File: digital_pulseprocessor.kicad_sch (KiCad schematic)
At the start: 26 parts, among them U300 SN74LV221AD, U301 SN74LV221AD, U305 74AC151M n.b.

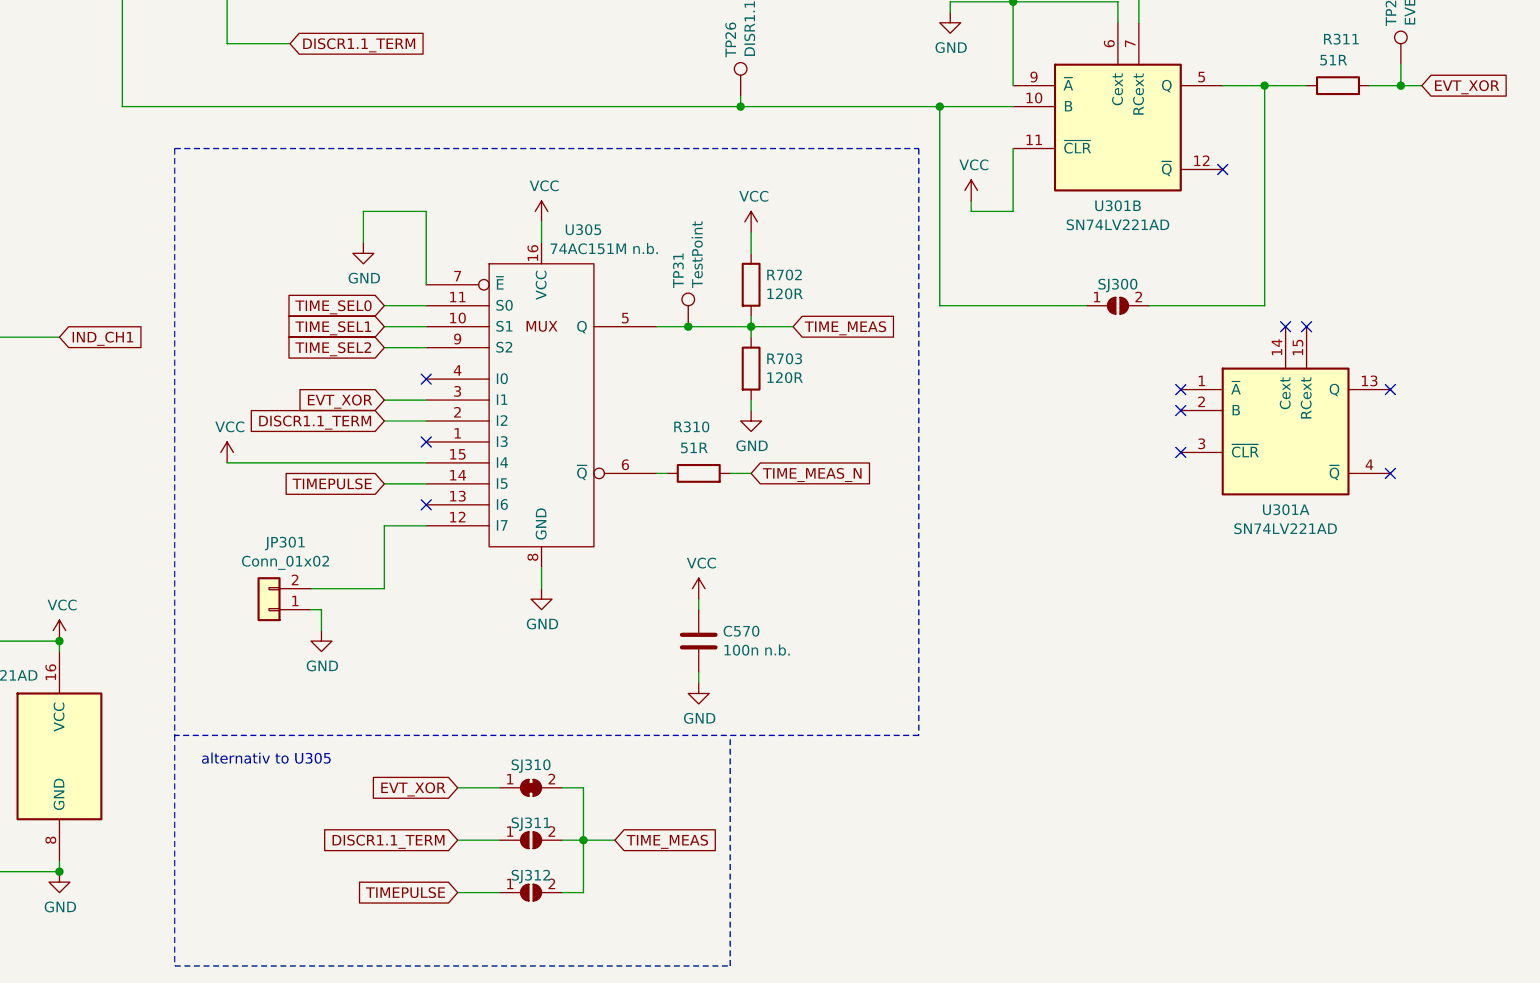
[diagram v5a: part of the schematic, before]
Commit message: Removed optionals parts. Cleaned up Schematics
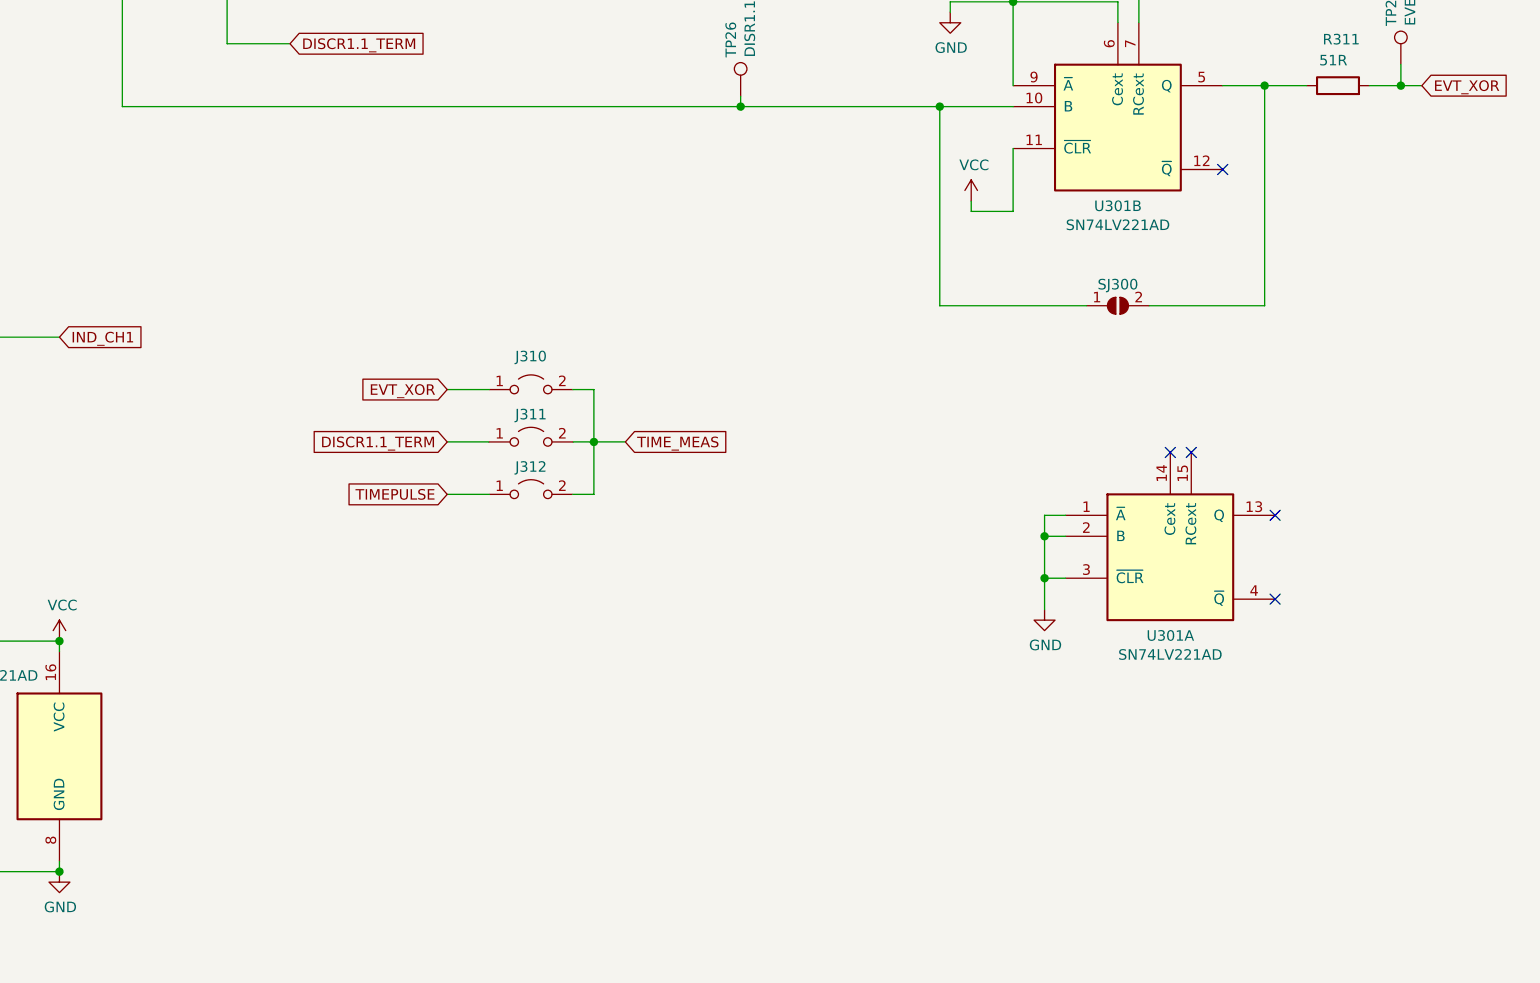
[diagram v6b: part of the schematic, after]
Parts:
- removed C570: 100n n.b., Capacitor_SMD:C_0805_2012Metric_Pad1.18x1.45mm_HandSolder, symbol Device:C
- removed JP301: Conn_01x02, Connector_PinHeader_2.54mm:PinHeader_1x02_P2.54mm_Vertical, symbol Connector_Generic:Conn_01x02
- removed R310: 51R, Resistor_SMD:R_0805_2012Metric_Pad1.20x1.40mm_HandSolder, symbol Device:R
- removed R702, R703: 120R, Resistor_SMD:R_0805_2012Metric_Pad1.20x1.40mm_HandSolder, symbol Device:R
- removed TP31: TestPoint, TestPoint:TestPoint_THTPad_1.5x1.5mm_Drill0.7mm, symbol Connector:TestPoint
- removed U305: 74AC151M n.b., Package_SO:SOP-16_3.9x9.9mm_P1.27mm, symbol muonpi-kicad-library:74AC151M
- J310: renamed from SJ310; footprint Jumper:SolderJumper-2_P1.3mm_Bridged_Pad1.0x1.5mm -> Connector_PinHeader_2.54mm:PinHeader_1x02_P2.54mm_Vertical; symbol Jumper:SolderJumper_2_Bridged -> Jumper:Jumper_2_Open; now in the parts list
- J311: renamed from SJ311; footprint Jumper:SolderJumper-2_P1.3mm_Open_Pad1.0x1.5mm -> Connector_PinHeader_2.54mm:PinHeader_1x02_P2.54mm_Vertical; symbol Jumper:SolderJumper_2_Open -> Jumper:Jumper_2_Open; now in the parts list
- J312: renamed from SJ312; footprint Jumper:SolderJumper-2_P1.3mm_Open_Pad1.0x1.5mm -> Connector_PinHeader_2.54mm:PinHeader_1x02_P2.54mm_Vertical; symbol Jumper:SolderJumper_2_Open -> Jumper:Jumper_2_Open; now in the parts list
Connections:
- net GND: now also U301.1 (~A), U301.2 (B), U301.3 (~CLR)
- no-connect marks 13 -> 7
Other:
- note removed: "alternativ to U305"
- moved on the sheet: U301A

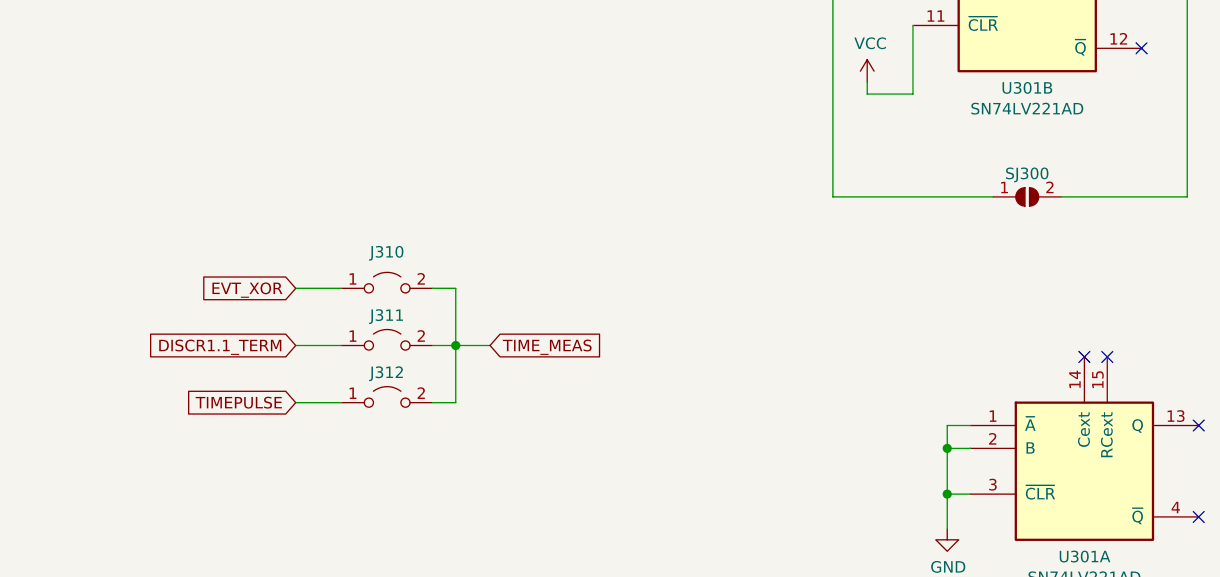
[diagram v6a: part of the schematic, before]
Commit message: Cleand all errors and warnings. Ready for review
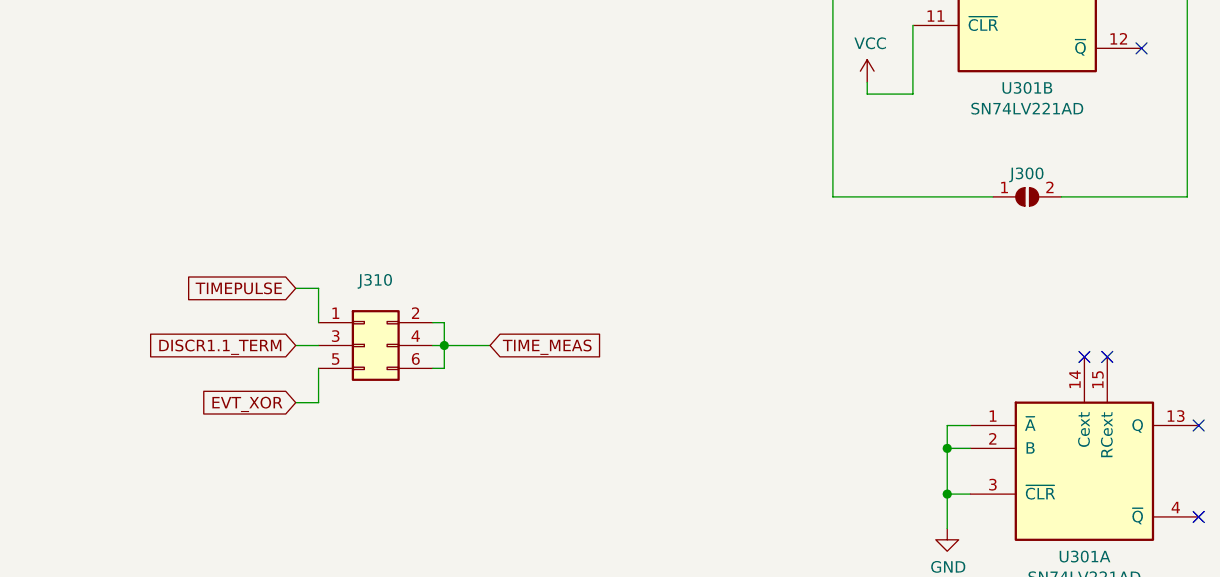
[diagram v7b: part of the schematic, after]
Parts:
- removed J310: Jumper_NC_Small, Connector_PinHeader_2.54mm:PinHeader_1x02_P2.54mm_Vertical, symbol Jumper:Jumper_2_Open
- removed J311, J312: Jumper_NO_Small, Connector_PinHeader_2.54mm:PinHeader_1x02_P2.54mm_Vertical, symbol Jumper:Jumper_2_Open
- added J310: Conn_02x03_Odd_Even, Connector_PinHeader_2.54mm:PinHeader_2x03_P2.54mm_Vertical, symbol Connector_Generic:Conn_02x03_Odd_Even
- J300: renamed from SJ300; now left out of the parts list
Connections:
- net DISCR1.1_TERM: now also J310.3 (Pin_3)
- net EVT_XOR: now also J310.5 (Pin_5)
- net TIMEPULSE: now also J310.1 (Pin_1)
- net TIME_MEAS: now also J310.2 (Pin_2), J310.4 (Pin_4), J310.6 (Pin_6)
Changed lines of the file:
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@@
   (junction (at 114.3 57.15) (diameter 1.016) (color 0 0 0 0))
   (junction (at 114.3 71.12) (diameter 1.016) (color 0 0 0 0))
-  (junction (at 158.75 129.54) (diameter 1.016) (color 0 0 0 0))
+  (junction (at 157.48 129.54) (diameter 1.016) (color 0 0 0 0))
   (junction (at 176.53 88.9) (diameter 1.016) (color 0 0 0 0))
   (junction (at 200.66 88.9) (diameter 1.016) (color 0 0 0 0))
@@
     (stroke (width 0) (type solid) (color 0 0 0 0))
   )
-  (wire (pts (xy 140.97 123.19) (xy 146.05 123.19))
-    (stroke (width 0) (type solid) (color 0 0 0 0))
-  )
-  (wire (pts (xy 140.97 129.54) (xy 146.05 129.54))
-    (stroke (width 0) (type solid) (color 0 0 0 0))
-  )
-  (wire (pts (xy 140.97 135.89) (xy 146.05 135.89))
-    (stroke (width 0) (type solid) (color 0 0 0 0))
-  )
-  (wire (pts (xy 156.21 123.19) (xy 158.75 123.19))
-    (stroke (width 0) (type solid) (color 0 0 0 0))
-  )
-  (wire (pts (xy 156.21 129.54) (xy 158.75 129.54))
-    (stroke (width 0) (type solid) (color 0 0 0 0))
-  )
-  (wire (pts (xy 156.21 135.89) (xy 158.75 135.89))
-    (stroke (width 0) (type solid) (color 0 0 0 0))
-  )
-  (wire (pts (xy 158.75 123.19) (xy 158.75 129.54))
-    (stroke (width 0) (type solid) (color 0 0 0 0))
-  )
-  (wire (pts (xy 158.75 129.54) (xy 158.75 135.89))
-    (stroke (width 0) (type solid) (color 0 0 0 0))
-  )
-  (wire (pts (xy 158.75 129.54) (xy 162.56 129.54))
+  (wire (pts (xy 140.97 123.19) (xy 143.51 123.19))
+    (stroke (width 0) (type solid) (color 0 0 0 0))
+  )
+  (wire (pts (xy 140.97 129.54) (xy 143.51 129.54))
+    (stroke (width 0) (type solid) (color 0 0 0 0))
+  )
+  (wire (pts (xy 140.97 135.89) (xy 143.51 135.89))
+    (stroke (width 0) (type solid) (color 0 0 0 0))
+  )
+  (wire (pts (xy 143.51 123.19) (xy 143.51 127))
+    (stroke (width 0) (type solid) (color 0 0 0 0))
+  )
+  (wire (pts (xy 143.51 135.89) (xy 143.51 132.08))
+    (stroke (width 0) (type solid) (color 0 0 0 0))
+  )
+  (wire (pts (xy 156.21 127) (xy 157.48 127))
+    (stroke (width 0) (type solid) (color 0 0 0 0))
+  )
+  (wire (pts (xy 156.21 129.54) (xy 157.48 129.54))
+    (stroke (width 0) (type solid) (color 0 0 0 0))
+  )
+  (wire (pts (xy 156.21 132.08) (xy 157.48 132.08))
+    (stroke (width 0) (type solid) (color 0 0 0 0))
+  )
+  (wire (pts (xy 157.48 127) (xy 157.48 129.54))
+    (stroke (width 0) (type solid) (color 0 0 0 0))
+  )
+  (wire (pts (xy 157.48 129.54) (xy 162.56 129.54))
+    (stroke (width 0) (type solid) (color 0 0 0 0))
+  )
+  (wire (pts (xy 157.48 132.08) (xy 157.48 129.54))
     (stroke (width 0) (type solid) (color 0 0 0 0))
   )
@@
     )
   )
-  (global_label "EVT_XOR" (shape input) (at 140.97 123.19 180)
+  (global_label "TIMEPULSE" (shape input) (at 140.97 123.19 180)
     (effects (font (size 1.27 1.27)) (justify right))
-    (property "Intersheet References" "${INTERSHEET_REFS}" (id 0) (at 129.05 123.2694 0)
+    (property "Intersheet References" "${INTERSHEET_REFS}" (id 0) (at 126.8729 123.1106 0)
       (effects (font (size 1.27 1.27)) (justify right) hide)
     )
@@
     )
   )
-  (global_label "TIMEPULSE" (shape input) (at 140.97 135.89 180)
+  (global_label "EVT_XOR" (shape input) (at 140.97 135.89 180)
     (effects (font (size 1.27 1.27)) (justify right))
-    (property "Intersheet References" "${INTERSHEET_REFS}" (id 0) (at 126.8729 135.8106 0)
+    (property "Intersheet References" "${INTERSHEET_REFS}" (id 0) (at 129.05 135.9694 0)
       (effects (font (size 1.27 1.27)) (justify right) hide)
     )
@@
   )
   (symbol (lib_id "Jumper:SolderJumper_2_Open") (at 222.25 113.03 0) (unit 1)
-    (in_bom yes) (on_board yes)
-    (property "Reference" "SJ300" (id 0) (at 222.25 110.4646 0))
+    (in_bom no) (on_board yes)
+    (property "Reference" "J300" (id 0) (at 222.25 110.4646 0))
     (property "Value" "SolderJumper_2_Open" (id 1) (at 222.25 110.236 0)
       (effects (font (size 1.27 1.27)) hide)
@@
     (pin "2")
   )
-  (symbol (lib_id "Jumper:Jumper_2_Open") (at 151.13 123.19 0) (unit 1)
-    (in_bom yes) (on_board yes)
-    (property "Reference" "J310" (id 0) (at 151.13 119.1768 0))
-    (property "Value" "Jumper_NC_Small" (id 1) (at 151.13 120.2182 0)
-      (effects (font (size 1.27 1.27)) hide)
-    )
-    (property "Footprint" "Connector_PinHeader_2.54mm:PinHeader_1x02_P2.54mm_Vertical" (id 2) (at 151.13 123.19 0)
-      (effects (font (size 1.27 1.27)) hide)
-    )
-    (property "Datasheet" "~" (id 3) (at 151.13 123.19 0)
-      (effects (font (size 1.27 1.27)) hide)
-    )
-    (pin "1")
-    (pin "2")
-  )
-  (symbol (lib_id "Jumper:Jumper_2_Open") (at 151.13 129.54 0) (unit 1)
-    (in_bom yes) (on_board yes)
-    (property "Reference" "J311" (id 0) (at 151.13 126.2126 0))
-    (property "Value" "Jumper_NO_Small" (id 1) (at 151.13 127.254 0)
-      (effects (font (size 1.27 1.27)) hide)
-    )
-    (property "Footprint" "Connector_PinHeader_2.54mm:PinHeader_1x02_P2.54mm_Vertical" (id 2) (at 151.13 129.54 0)
-      (effects (font (size 1.27 1.27)) hide)
-    )
-    (property "Datasheet" "~" (id 3) (at 151.13 129.54 0)
-      (effects (font (size 1.27 1.27)) hide)
-    )
-    (pin "1")
-    (pin "2")
-  )
-  (symbol (lib_id "Jumper:Jumper_2_Open") (at 151.13 135.89 0) (unit 1)
-    (in_bom yes) (on_board yes)
-    (property "Reference" "J312" (id 0) (at 151.13 132.5626 0))
-    (property "Value" "Jumper_NO_Small" (id 1) (at 151.13 133.604 0)
-      (effects (font (size 1.27 1.27)) hide)
-    )
-    (property "Footprint" "Connector_PinHeader_2.54mm:PinHeader_1x02_P2.54mm_Vertical" (id 2) (at 151.13 135.89 0)
-      (effects (font (size 1.27 1.27)) hide)
-    )
-    (property "Datasheet" "~" (id 3) (at 151.13 135.89 0)
-      (effects (font (size 1.27 1.27)) hide)
-    )
-    (pin "1")
-    (pin "2")
-  )
   (symbol (lib_id "Device:C") (at 24.13 167.64 0) (unit 1)
     (in_bom yes) (on_board yes)
@@
     (pin "2")
   )
+  (symbol (lib_id "Connector_Generic:Conn_02x03_Odd_Even") (at 148.59 129.54 0) (unit 1)
+    (in_bom yes) (on_board yes) (fields_autoplaced)
+    (property "Reference" "J310" (id 0) (at 149.86 122.2968 0))
+    (property "Value" "Conn_02x03_Odd_Even" (id 1) (at 149.86 124.5955 0)
+      (effects (font (size 1.27 1.27)) hide)
+    )
+    (property "Footprint" "Connector_PinHeader_2.54mm:PinHeader_2x03_P2.54mm_Vertical" (id 2) (at 148.59 129.54 0)
+      (effects (font (size 1.27 1.27)) hide)
+    )
+    (property "Datasheet" "~" (id 3) (at 148.59 129.54 0)
+      (effects (font (size 1.27 1.27)) hide)
+    )
+    (pin "1")
+    (pin "2")
+    (pin "3")
+    (pin "4")
+    (pin "5")
+    (pin "6")
+  )
   (symbol (lib_id "74xx:74LS221") (at 44.45 167.64 0) (unit 3)
